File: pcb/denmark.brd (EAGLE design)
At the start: 100 x 90 mm, 81 parts, among them IC1 74AHC1G32DBV, IC2 REG1117, U2 MB85RCSOIC8, X1 22-23-2021, X2 22-23-2031, X3 22-23-2051, X4 22-23-2021

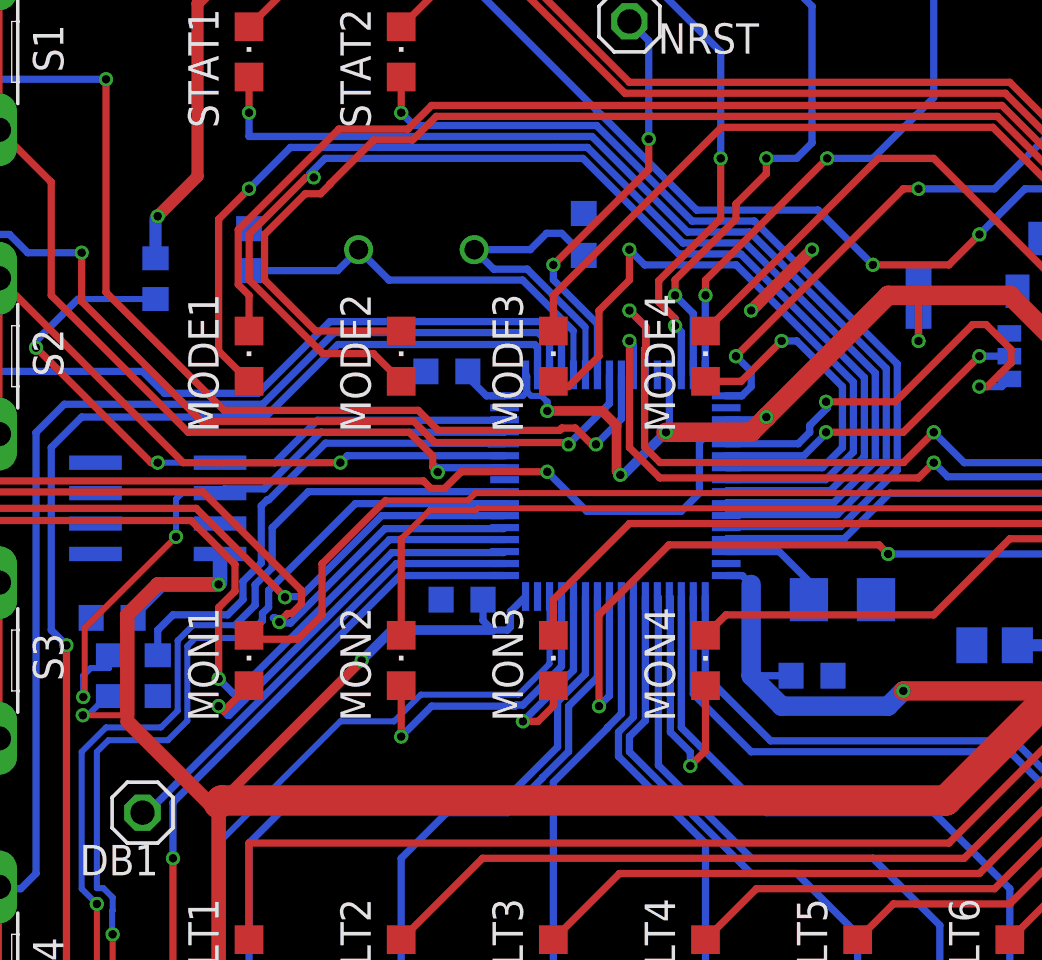
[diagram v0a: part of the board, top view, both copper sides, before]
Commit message: Update MCU footprint and add BOM
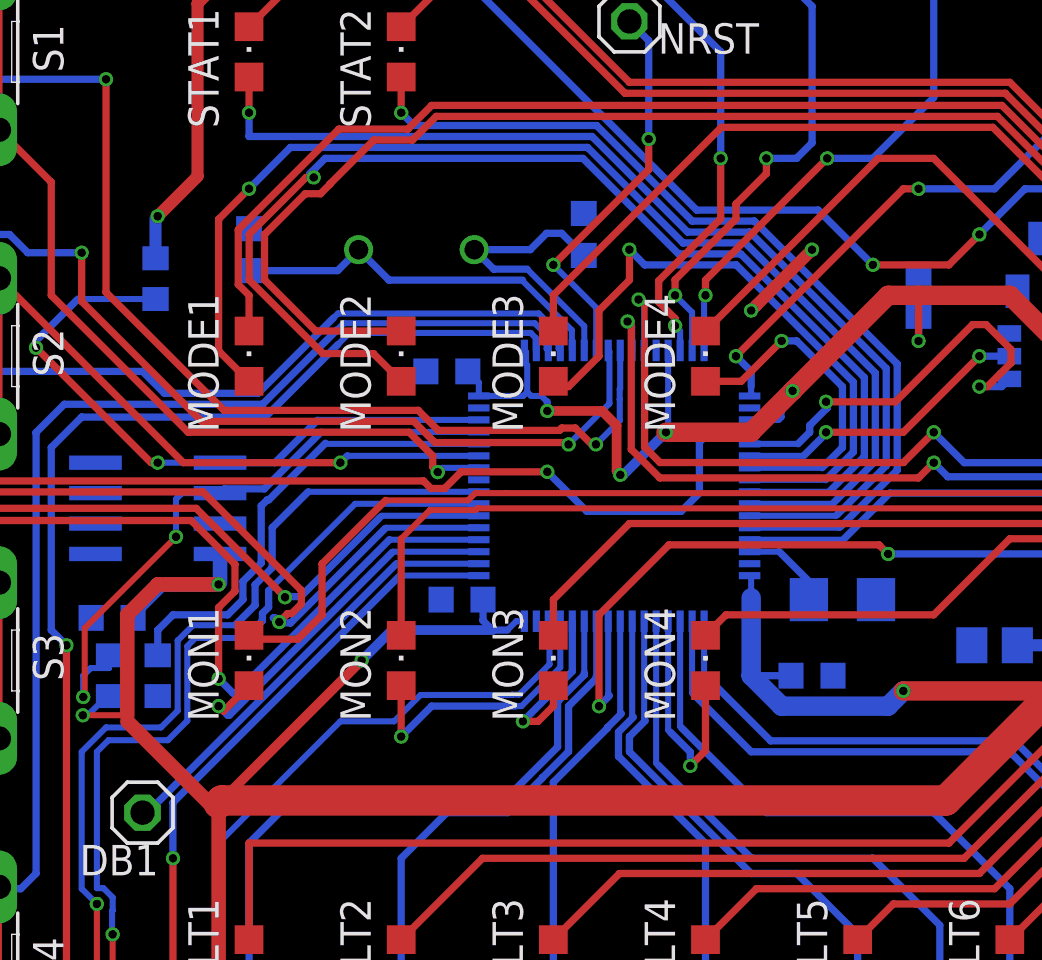
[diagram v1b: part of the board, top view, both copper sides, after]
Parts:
- C12, C4: value 100n -> 20n
- U$1: value STM32F4R_64PIN_FOXCAR -> STM32F4_10X10_LQFP64; device stm32f4:LQFP64 -> stm32f4:LQFP-ST-64-2
- moved U$1 0.33 mm to (-58.4, -34.6), turned to 270 degrees
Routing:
- net BUTTON1_INPUT: track 37.1 -> 35.6 mm
- net I2C_SDA: track 28.3 -> 27.2 mm
- net LED_MONITOR_1: track 16.7 -> 15.6 mm
- net SWO: track 58.5 -> 57.4 mm
- net SOFTCLIP_LF_AMP: track 54.0 -> 52.9 mm
- net MUTE_MF_AMP: track 33.9 -> 32.9 mm
- net I2C_SCL: track 27.4 -> 26.3 mm
- net SWCLK: track 56.9 -> 55.8 mm
- net STANDBY_LF_AMP: track 43.2 -> 42.1 mm
- net N$43: track 19.4 -> 18.3 mm
- net JTRST: track 72.5 -> 71.4 mm
- net BUTTON2_INPUT: track 30.9 -> 29.8 mm
- net LED_MONITOR_2: track 12.9 -> 11.9 mm
- net LED_FAULT_2: track 25.6 -> 24.5 mm
- net LED_FAULT_1: track 31.7 -> 30.6 mm
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
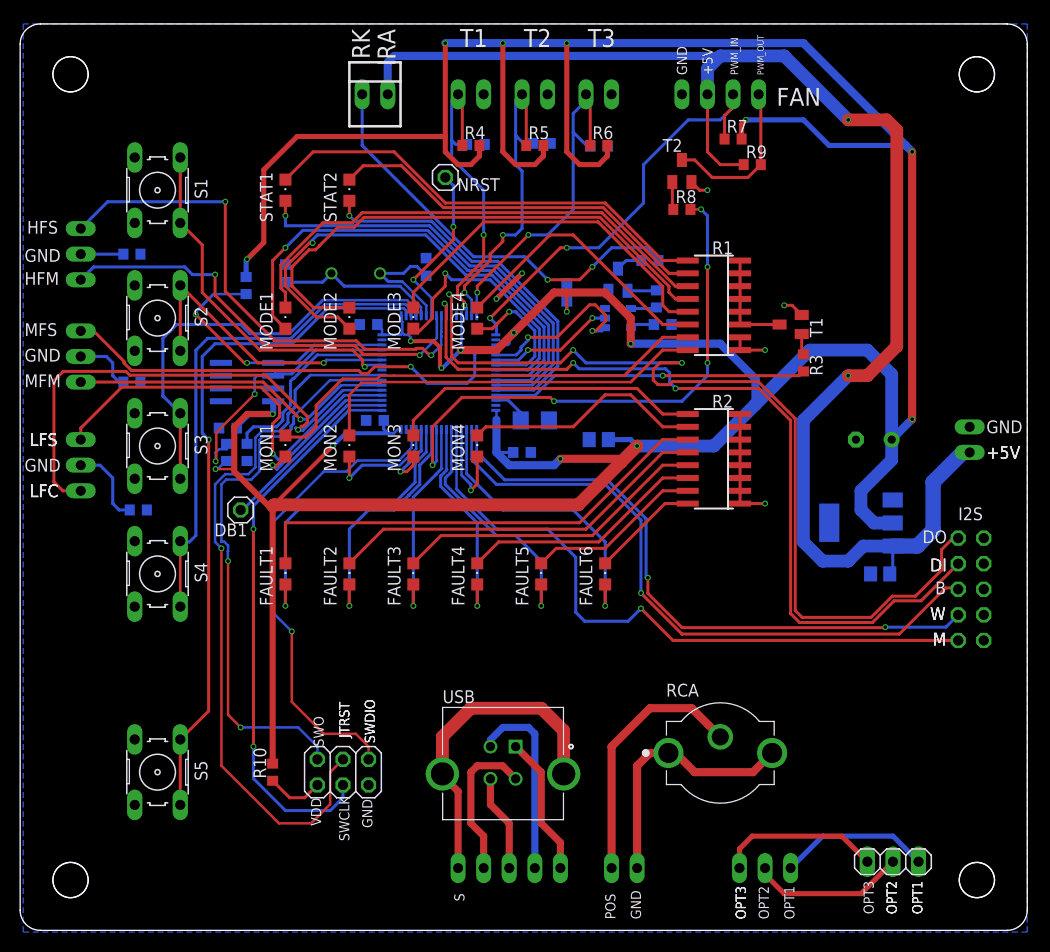
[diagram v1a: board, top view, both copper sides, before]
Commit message: Update BOM and PCB to incorporate reworks
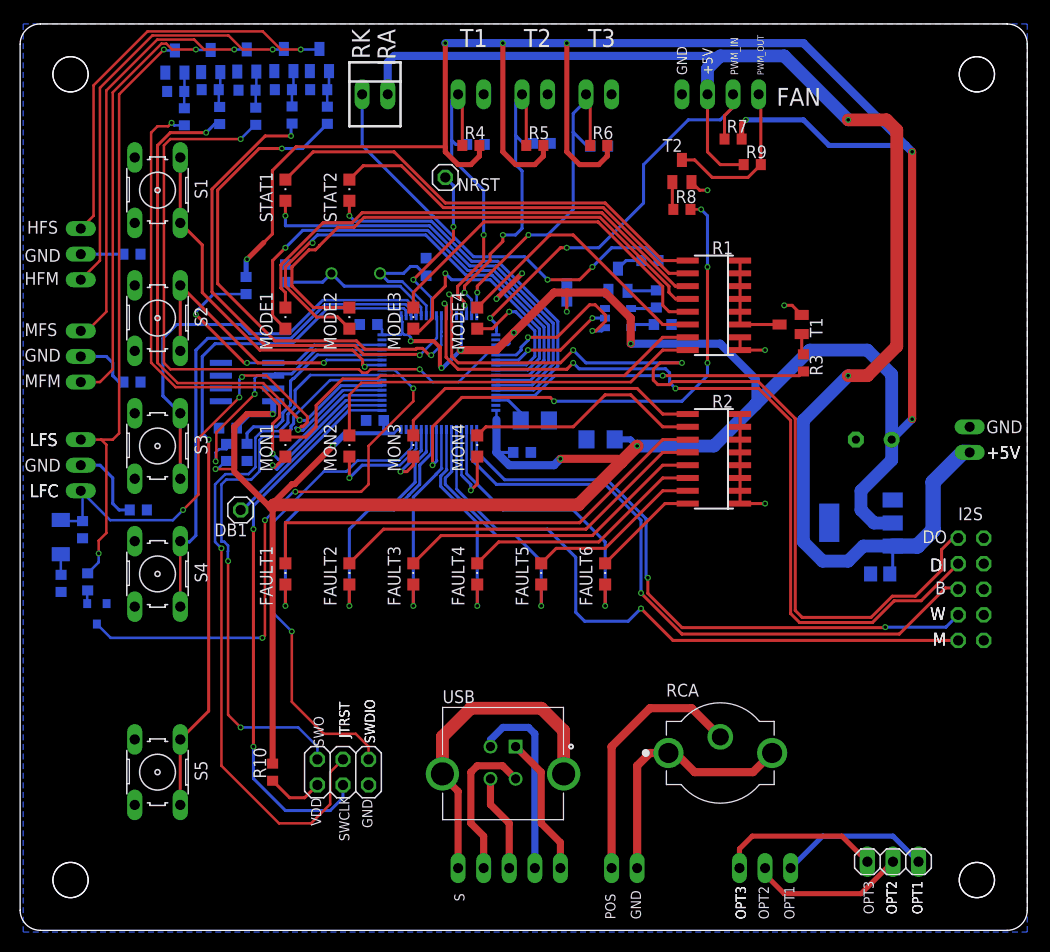
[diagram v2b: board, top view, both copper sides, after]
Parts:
- added D1: (no value), diode:SOD80C
- added R19, R21, R23, R24, R26, R31: 10k, rcl:R0603
- added R20, R22, R25, R27, R28: 2.7k, rcl:R0603
- added R29, R30: 330, rcl:R0603
- added T4, T5, T6, T7, T9: (no value), transistor:SOT23-BEC
- added T8: (no value), zetex:SOT-23
- C11: value 4.7u -> 4.7u <1.0 ESR; device rcl:C0805 -> rcl:C1206
- R12: value 1k -> 470
- R13: value 1k -> 220
- moved C11 0.18 mm to (-42.4, -41.2)
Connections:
- new net N$18: HF_AMP.3, T4.C
- new net N$19: R19.1, R20.1, T4.B
- new net N$20: HF_AMP.1, T9.C
- new net N$21: R21.1, R22.1, T9.B
- new net N$22: LF_AMP.3, R31.1, T7.C
- new net N$23: MF_AMP.3, T5.C
- new net N$24: R24.1, R25.1, T5.B
- new net N$27: MF_AMP.1, T6.C
- new net N$28: R26.1, R27.1, T6.B
- new net N$29: R23.1, R28.1, T7.B
- new net N$35: R31.2, T8.3
- new net N$41: D1.A, R30.1
- new net STANDBY_LF_AMP_MONITOR: T8.1, U$1.57
- net GND: now also R19.2, R21.2, R23.2, R24.2, R26.2, R29.2, R30.2, T4.E, T5.E, T6.E, T7.E, T8.2, T9.E
- net MUTE_HF_AMP: now also R22.2; no longer HF_AMP.1
- net MUTE_MF_AMP: now also R27.2; no longer MF_AMP.1
- net SOFTCLIP_LF_AMP: now also D1.C, R29.1
- net STANDBY_HF_AMP: now also R20.2; no longer HF_AMP.3
- net STANDBY_LF_AMP: now also R28.2; no longer LF_AMP.3
- net STANDBY_MF_AMP: now also R25.2; no longer MF_AMP.3
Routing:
- net N$22: track 0.00 -> 59.4 mm, vias 0 -> 2
- net STANDBY_LF_AMP_MONITOR: track 0.00 -> 55.8 mm, vias 0 -> 4
- net N$27: track 0.00 -> 43.2 mm, vias 0 -> 1
- net N$23: track 0.00 -> 41.7 mm, vias 0 -> 1
- net N$20: track 0.00 -> 40.9 mm, vias 0 -> 1
- net N$18: track 0.00 -> 40.2 mm, vias 0 -> 1
- net MUTE_MF_AMP: track 32.9 -> 55.1 mm, vias 1 -> 2
- net STANDBY_MF_AMP: track 46.7 -> 66.9 mm, vias 1 -> 2
- net STANDBY_LF_AMP: track 42.1 -> 60.0 mm, vias 1 -> 2
- net MUTE_HF_AMP: track 43.7 -> 49.4 mm
- net N$24: track 0.00 -> 3.62 mm
- net N$19: track 0.00 -> 3.62 mm
- net N$21: track 0.00 -> 3.58 mm
- net N$28: track 0.00 -> 3.56 mm
- net N$29: track 0.00 -> 3.55 mm
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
